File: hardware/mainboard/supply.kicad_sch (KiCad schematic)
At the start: 58 parts, among them Q2 STL130N4LF8, U16 SPX5205M5-L_TR, U19 L7987, U3 L5973D, U6 SPX5205M5-L_TR, U7 SPX5205M5-L_TR, U9 SPX5205M5-L_TR

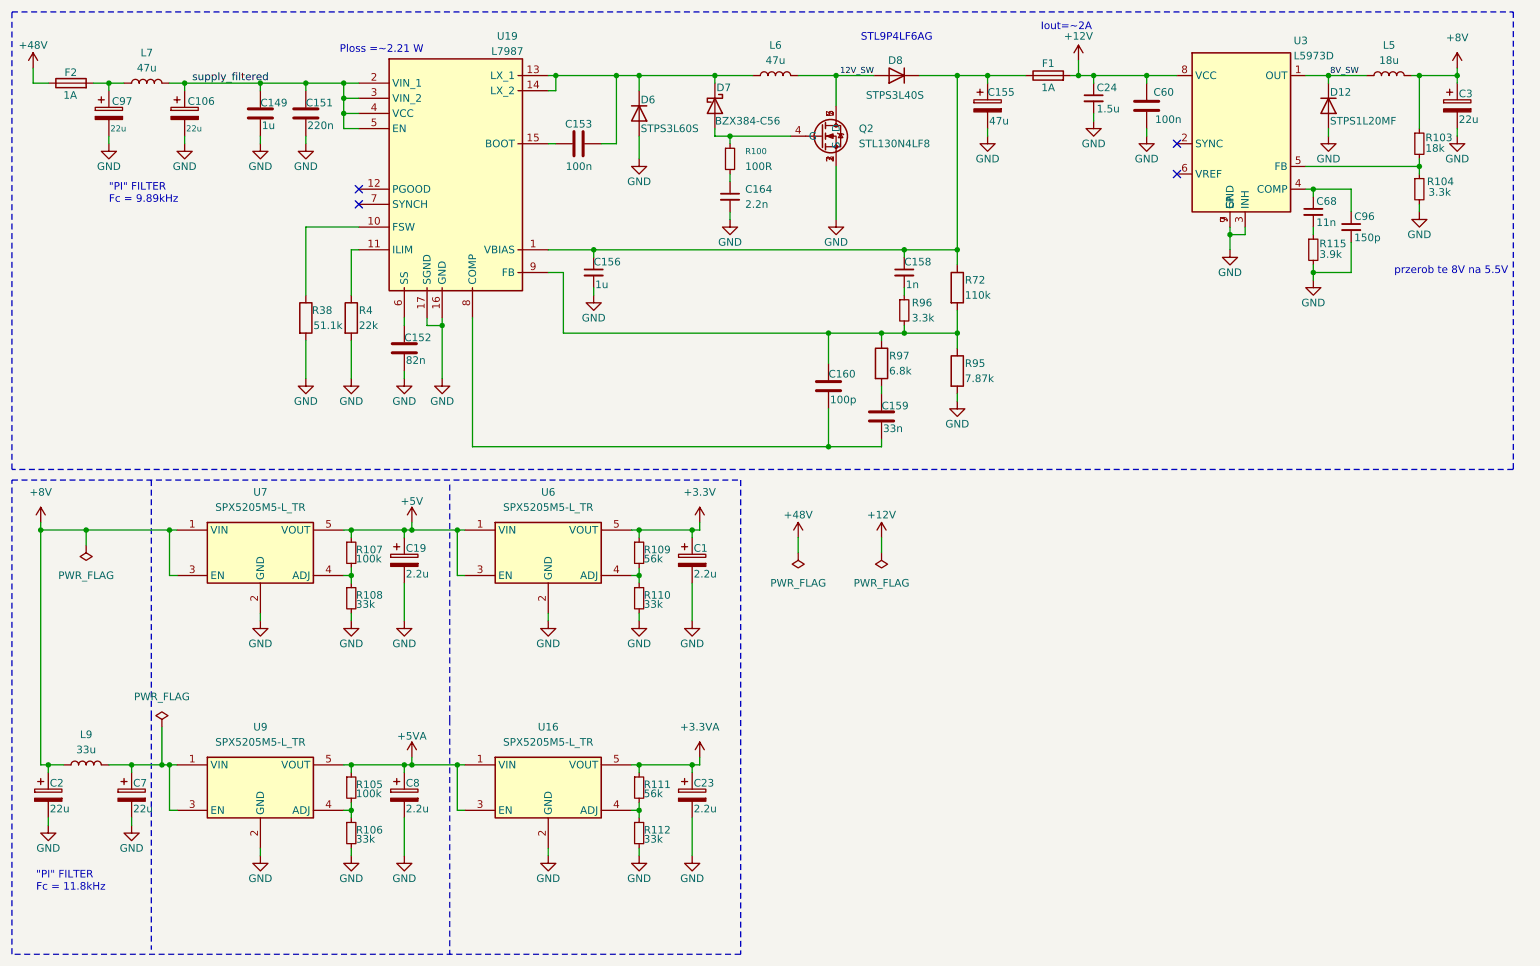
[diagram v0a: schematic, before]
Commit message: Add power supply and front panel PCBs
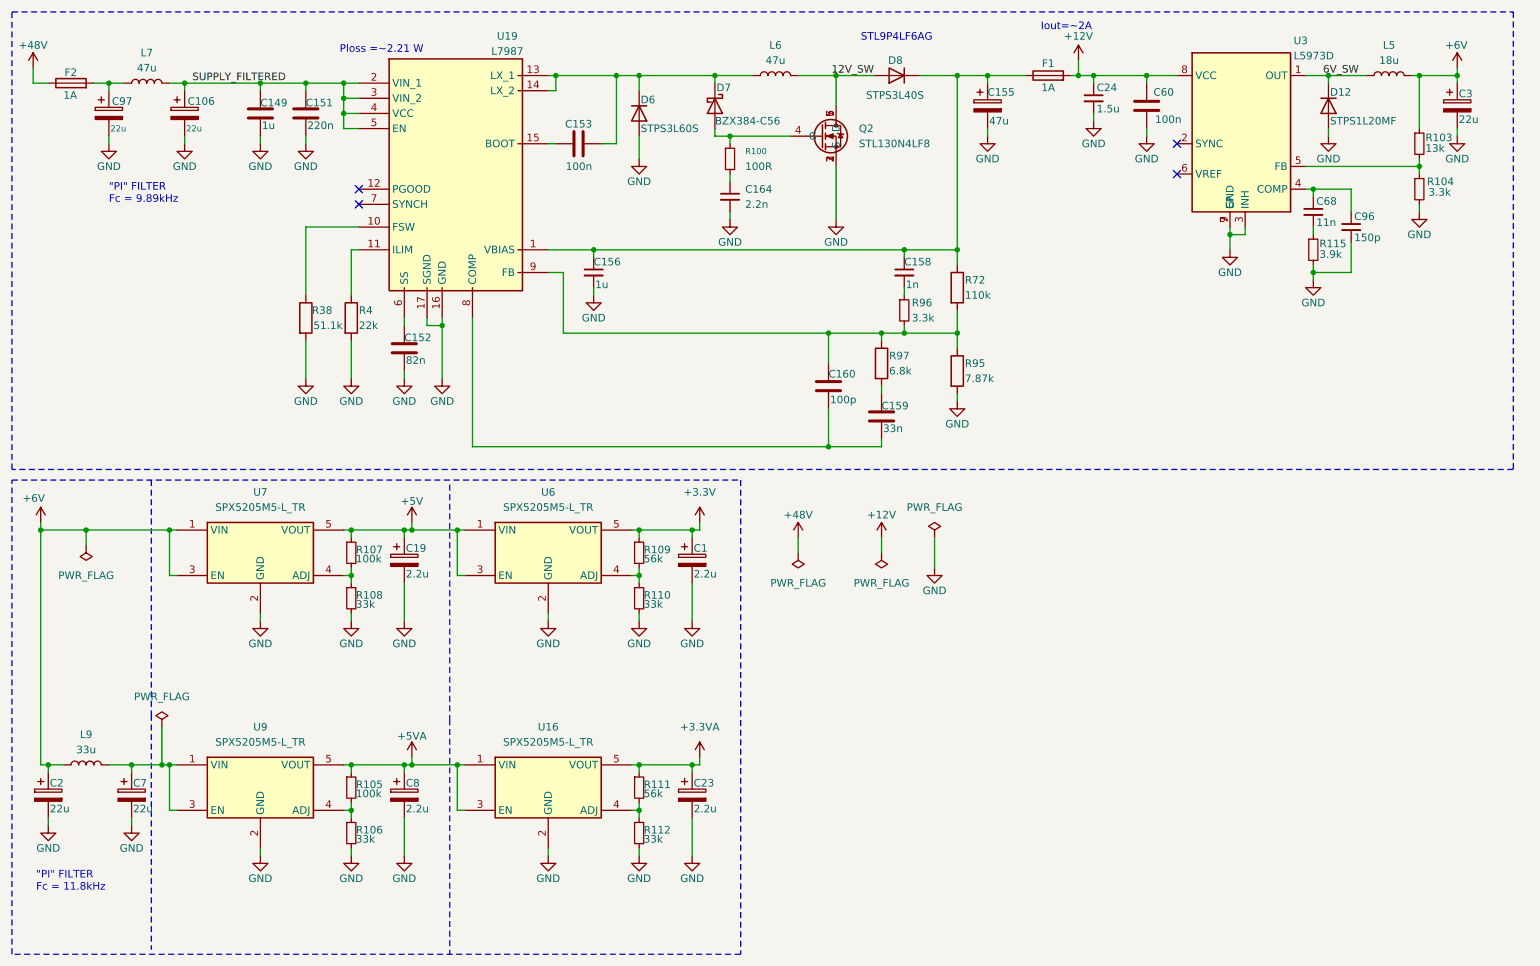
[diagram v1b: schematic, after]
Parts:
- removed U16, U6, U7, U9: SPX5205M5-L_TR, digital_amp:SOT95P280X145-5N, symbol psd_libs:SPX5205M5-L_TR
- added U16, U6, U7, U9: SPX5205M5-L_TR, digital_amp:SOT95P280X145-5N, symbol digital_amp:SPX5205M5-L_TR
- R103: value 18k -> 13k
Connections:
- net +3.3V: now also U6.5 (VOUT)
- net +3.3VA: now also U16.5 (VOUT)
- net +5V: now also U6.1 (VIN), U6.3 (EN), U7.5 (VOUT)
- net +5VA: now also U16.1 (VIN), U16.3 (EN), U9.5 (VOUT)
- net GND: now also U16.2 (GND), U6.2 (GND), U7.2 (GND), U9.2 (GND)
- net at R107.2, R108.1: now also U7.4 (ADJ)
- net at C7.1, L9.2: now also U9.1 (VIN), U9.3 (EN)
- net at R105.2, R106.1: now also U9.4 (ADJ)
- net at R109.2, R110.1: now also U6.4 (ADJ)
- net at R111.2, R112.1: now also U16.4 (ADJ)
- net +8V renamed +6V
- net +6V: now also U7.1 (VIN), U7.3 (EN)
- net 8V_SW renamed 6V_SW
- net supply_filtered renamed SUPPLY_FILTERED
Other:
- note removed: "przerob te 8V na 5.5V"

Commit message: Prepare PCB for production
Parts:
- C149, C156: Manufacturer_Part_Number (none) -> CL10A105KB8NNNC
- C151: Manufacturer_Part_Number (none) -> CL10B224KO8NNNC
- C152: Manufacturer_Part_Number (none) -> C0603C823K5RACTU
- C153, C60: Manufacturer_Part_Number (none) -> 0603B104K500CT
- C158: Manufacturer_Part_Number (none) -> 0603B102K500CT
- C159: Manufacturer_Part_Number (none) -> CC0603JRX7R9BB333
- C160: Manufacturer_Part_Number (none) -> CL10C101JB8NNNC
- C164: Manufacturer_Part_Number (none) -> GRM1885C1H222JA01D
- D12: Manufacturer_Part_Number (none) -> STPS1L20MF
- D6: Manufacturer_Part_Number (none) -> STPS3L60S
- D7: Manufacturer_Part_Number (none) -> BZX384-C56
- D8: Manufacturer_Part_Number (none) -> STPS3L40S
- L5: Manufacturer_Part_Number 744776118 -> 744776118
- R100: Manufacturer_Part_Number (none) -> WR06X1000FTL
- R115: Manufacturer_Part_Number RC0402BR-07220KL -> RC0402BR-07220KL
- R38: Manufacturer_Part_Number (none) -> ERJ3EKF5112V
- R4: Manufacturer_Part_Number (none) -> WR06X2202FTL
- R72: Manufacturer_Part_Number (none) -> ERJ3GEYJ114V
- R95: Manufacturer_Part_Number (none) -> ERJ3EKF7871V
- R96: Manufacturer_Part_Number (none) -> ERA-2ARC2612X
- R97: Manufacturer_Part_Number (none) -> RC0603FR-076K8L
- U3: Manufacturer_Part_Number (none) -> L5973D013TR
